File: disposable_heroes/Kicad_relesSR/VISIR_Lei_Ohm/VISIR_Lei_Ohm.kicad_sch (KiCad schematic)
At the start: 4 parts, among them K1 3572-1220-053

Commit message: update kicad
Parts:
- removed K1: 3572-1220-053, RELAY8_3572-1220-053_COM, symbol rele_DPST_Tese:3572-1220-053
- added J1: Raspberry_Pi_2_3, symbol Connector:Raspberry_Pi_2_3
- added K1: 3572-1220-123, RELAY8_3572-1220-053_COM, symbol 3572-1220-123:3572-1220-123
- added U1: 4N35, Package_DIP:DIP-6_W7.62mm, symbol Isolator:4N35
- added U2: ULN2003, symbol Transistor_Array:ULN2003
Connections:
- net at R2.1, R3.1: now also K1.8; no longer R1.1
- new net: K1.14, R1.1
- new net: K1.1, R1.2
- new net: K1.6, U2.16 (O1)
- new net: K1.7, R2.2
- new net +12V: K1.2, U2.9 (COM)
- new net GND: U2.8 (GND)
- now unconnected: R3.2
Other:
- moved on the sheet: R1, R2, R3

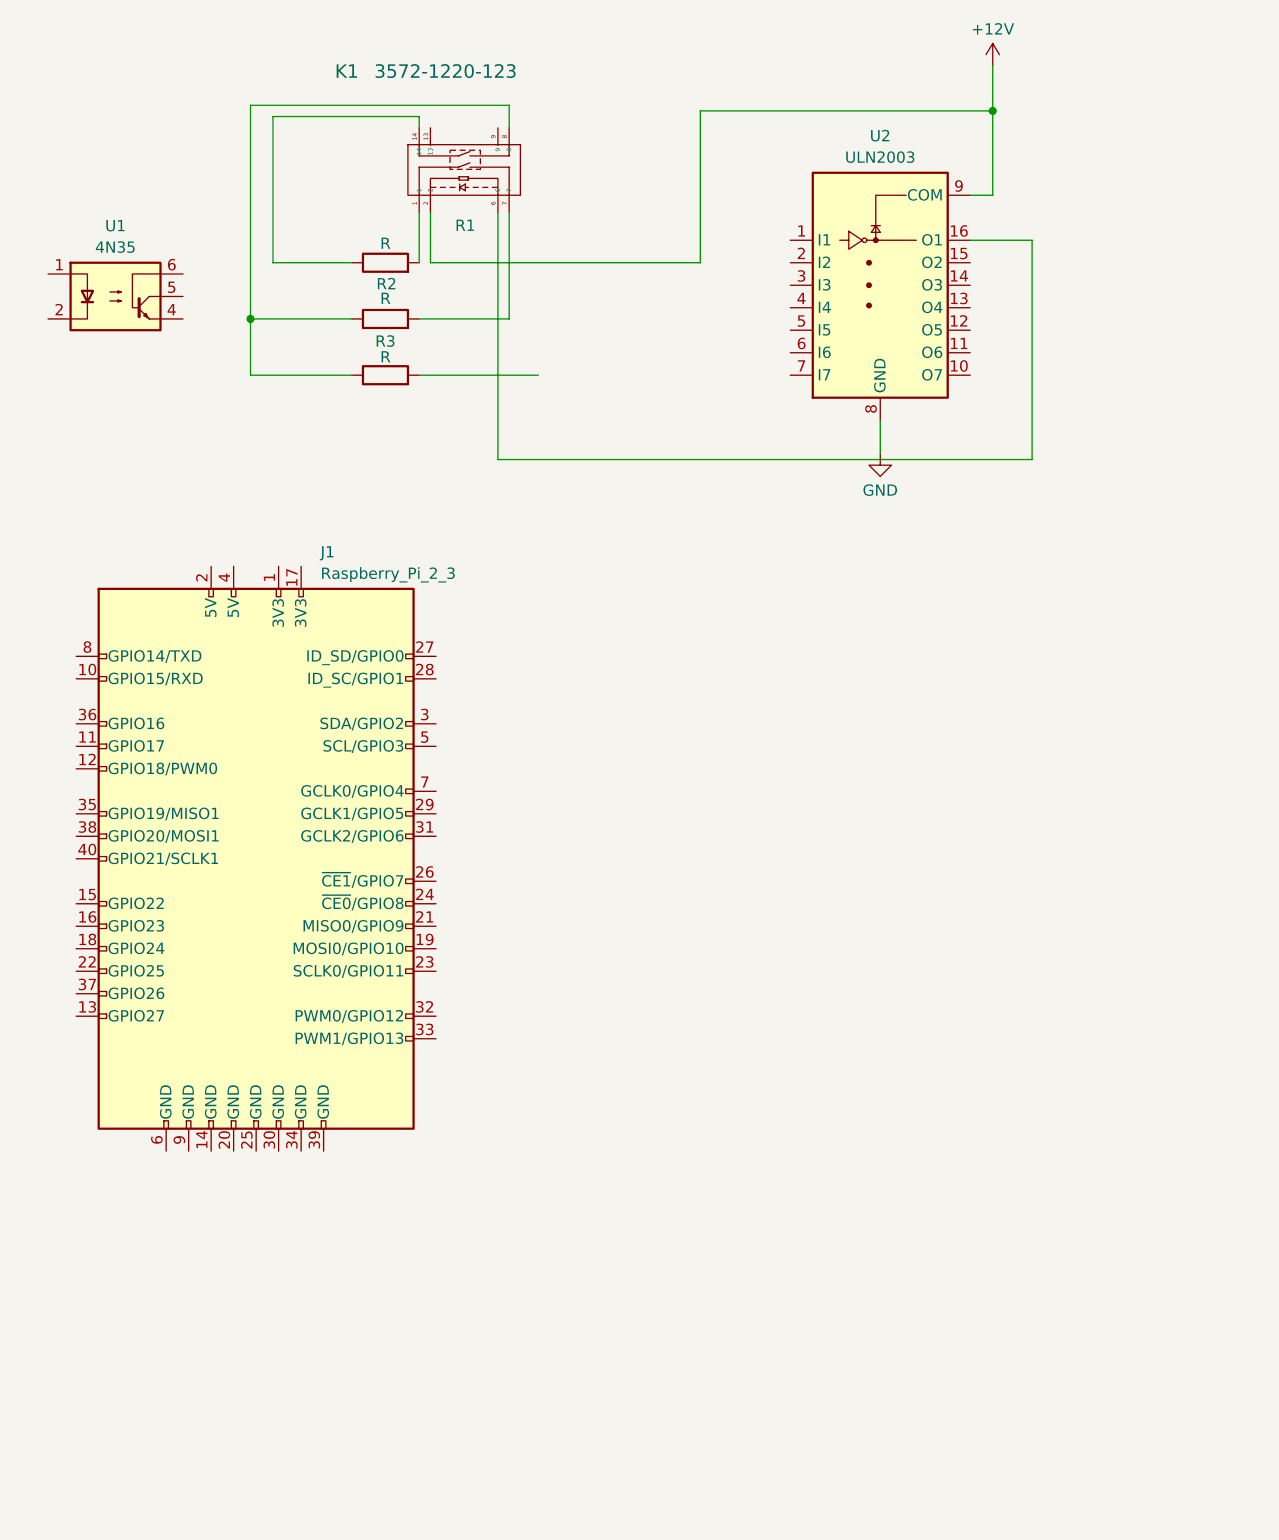
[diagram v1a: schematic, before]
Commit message: Kicad_Lei de Ohm
Parte do esquema de comando da Lei de Ohm
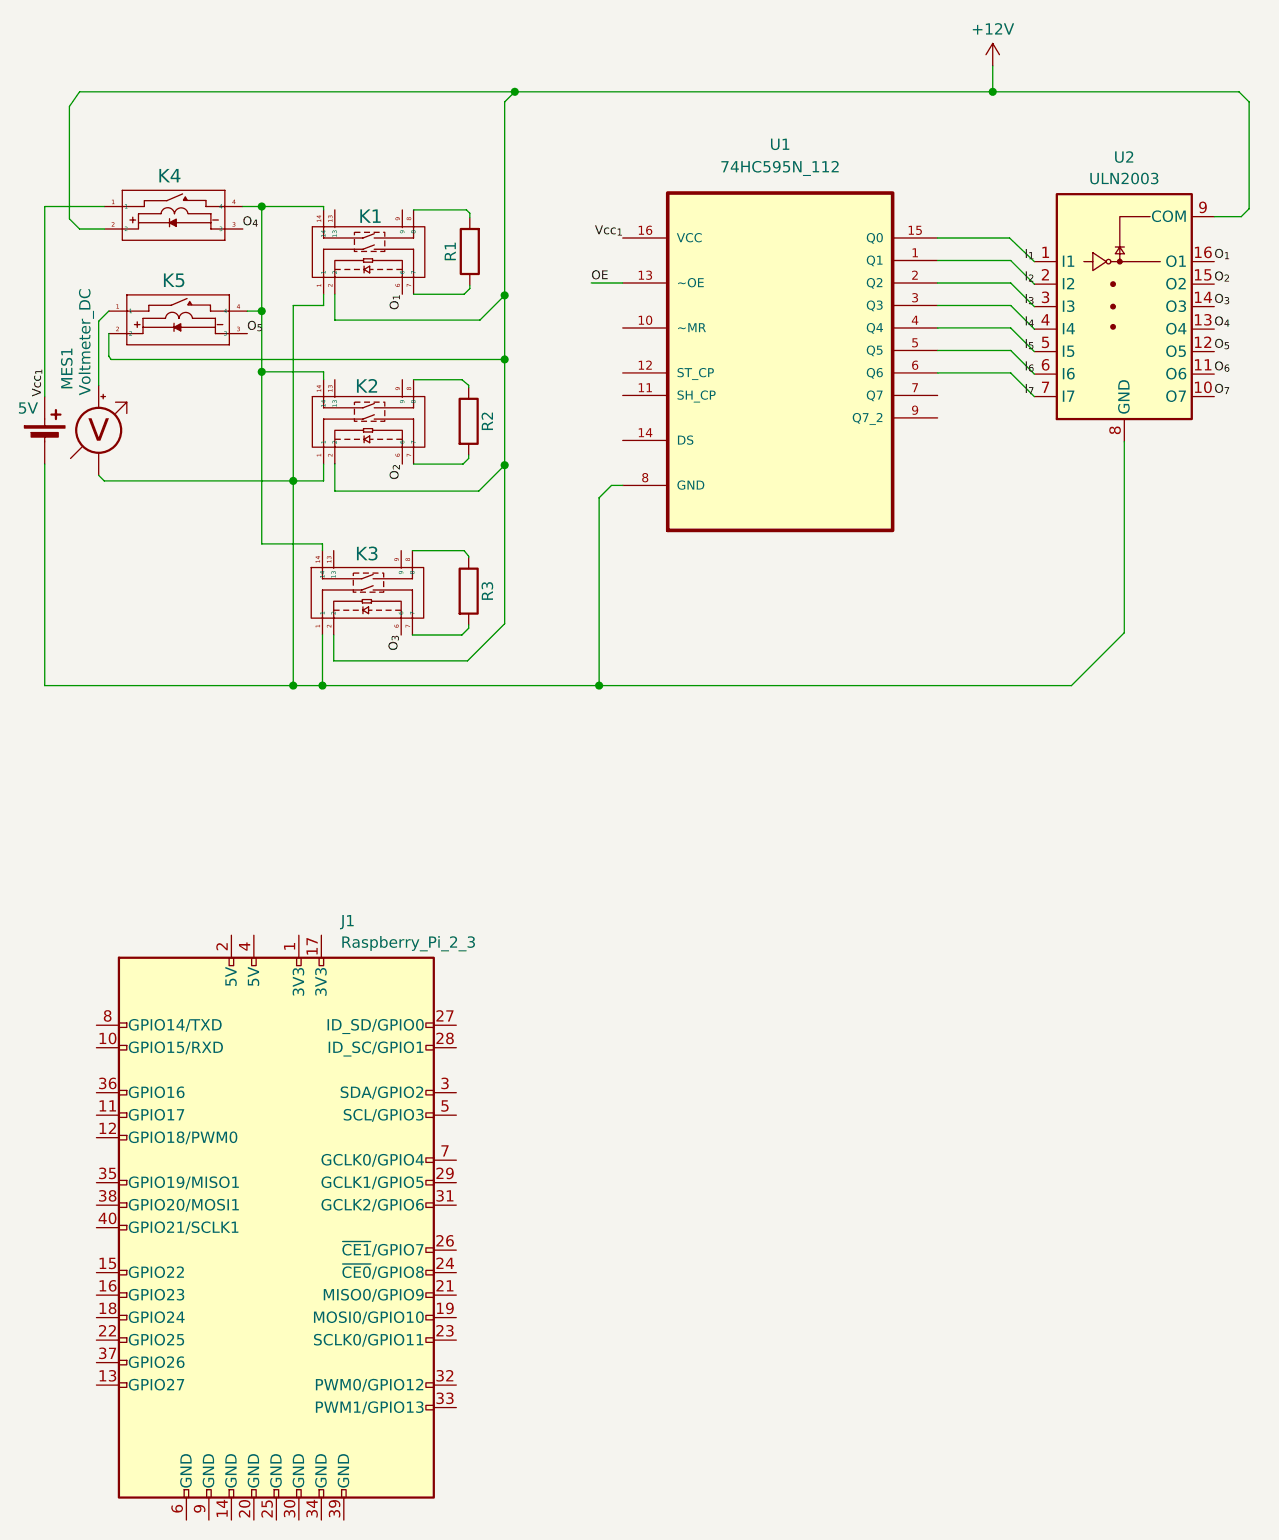
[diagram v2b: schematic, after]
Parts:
- removed U1: 4N35, Package_DIP:DIP-6_W7.62mm, symbol Isolator:4N35
- added K2, K3: 3572-1220-123, rele_DPST_tese:RELAY8_3572-1220-053_COM, symbol 3572-1220-123:3572-1220-123
- added K4, K5: 3570-1331-123, rele_SPST_tese:SIP_3570-1331_COM, symbol 3570-1331-123:3570-1331-123
- added MES1: Voltmeter_DC, Connector_PinHeader_2.54mm:PinHeader_1x02_P2.54mm_Vertical, symbol Device:Voltmeter_DC
- added U1: 74HC595N_112, Package_DIP:DIP-16_W10.16mm, symbol 74HC595N:74HC595N_112
- added Vcc1: 5V, Connector_PinHeader_2.54mm:PinHeader_1x02_P2.54mm_Vertical, symbol Device:Battery_Cell
- J1: footprint (none) -> Connector_PinHeader_2.54mm:PinHeader_2x39_P2.54mm_Vertical
- K1: footprint RELAY8_3572-1220-053_COM -> rele_DPST_tese:RELAY8_3572-1220-053_COM
- R1: value R -> R1; footprint (none) -> Resistor_THT:R_Axial_DIN0207_L6.3mm_D2.5mm_P15.24mm_Horizontal
- R2: value R -> R2; footprint (none) -> Resistor_THT:R_Axial_DIN0207_L6.3mm_D2.5mm_P15.24mm_Horizontal
- R3: value R -> R3; footprint (none) -> Resistor_THT:R_Axial_DIN0207_L6.3mm_D2.5mm_P15.24mm_Horizontal
- U2: footprint (none) -> Package_DIP:DIP-16_W10.16mm
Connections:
- net +12V: now also K2.2, K3.2, K4.2, K5.2
- net at R1.1: now also K1.7; no longer K1.14
- net at R1.2: now also K1.8; no longer K1.1
- net I_{1}: now reaches U2.1 (I1)
- net I_{1}: now also U1.15 (Q0)
- net O_{7}: now reaches U2.10 (O7)
- net O_{6}: now reaches U2.11 (O6)
- net O_{5}: now reaches U2.12 (O5)
- net O_{4}: now reaches U2.13 (O4)
- net O_{3}: now reaches U2.14 (O3)
- net O_{3}: now also K3.6
- net O_{2}: now reaches U2.15 (O2)
- net O_{2}: now also K2.6
- net O_{1}: now reaches K1.6, U2.16 (O1)
- net I_{2}: now reaches U2.2 (I2)
- net I_{2}: now also U1.1 (Q1)
- net I_{3}: now reaches U2.3 (I3)
- net I_{3}: now also U1.2 (Q2)
- net I_{4}: now reaches U2.4 (I4)
- net I_{4}: now also U1.3 (Q3)
- net I_{5}: now reaches U2.5 (I5)
- net I_{5}: now also U1.4 (Q4)
- net I_{6}: now reaches U2.6 (I6)
- net I_{6}: now also U1.5 (Q5)
- net I_{7}: now reaches U2.7 (I7)
- net I_{7}: now also U1.6 (Q6)
- net at R2.2: now also K2.7; no longer K1.7
- net at R3.2: now also K3.7
- net GND: no longer names the net of U2.8 (GND)
- net GND: now also K1.1, K2.1, K3.1, MES1.1 (-), U1.8 (GND), Vcc1.2 (-)
- new net: K5.1, MES1.2 (+)
- new net: K1.14, K2.14, K3.14, K4.4, K5.4
- new net: K3.8, R3.1
- new net: K2.8, R2.1
- new net OE: U1.13 (~OE)
- new net Vcc_{1}: K4.1, U1.16 (VCC), Vcc1.1 (+)
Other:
- moved on the sheet: J1, K1, U2

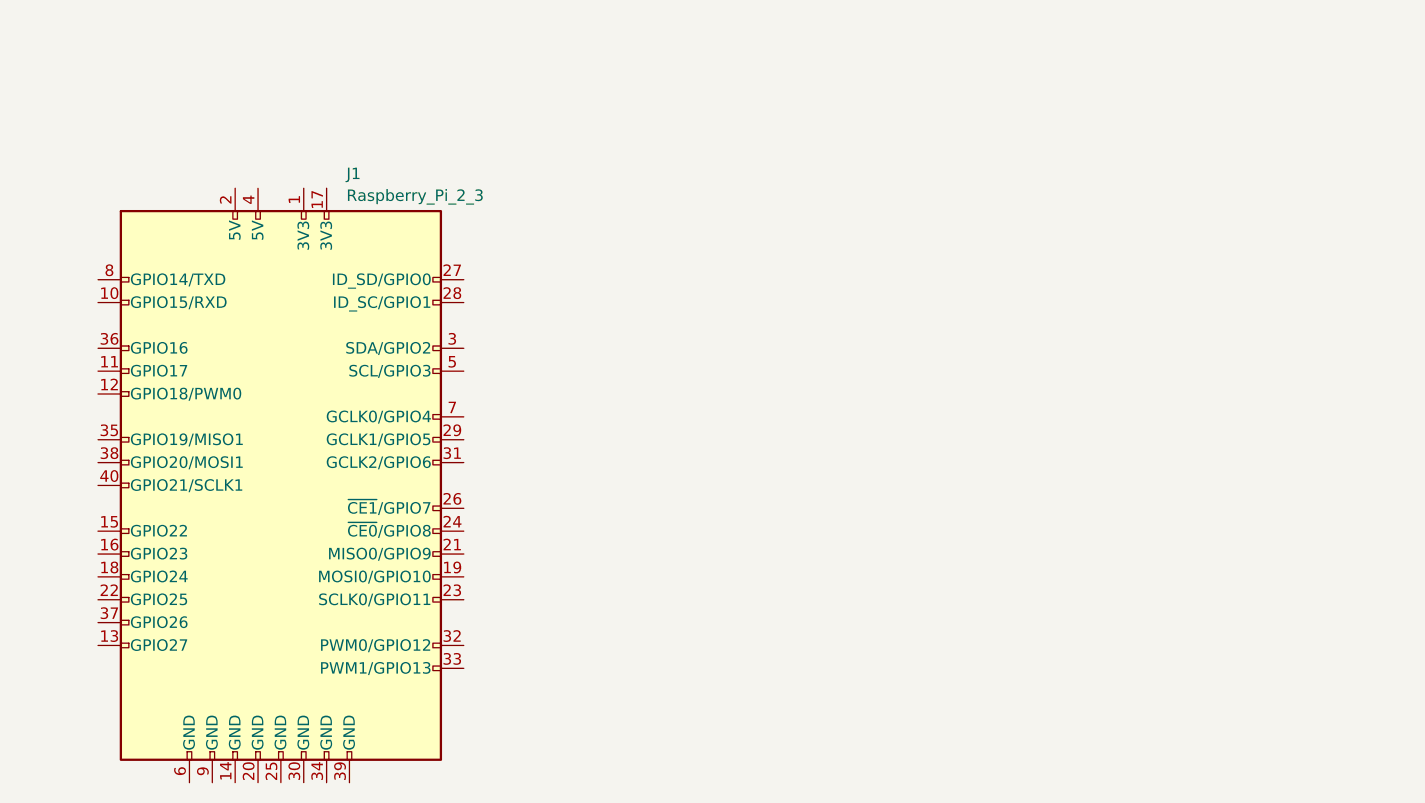
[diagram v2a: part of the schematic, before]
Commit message: kicad pi5 symbol
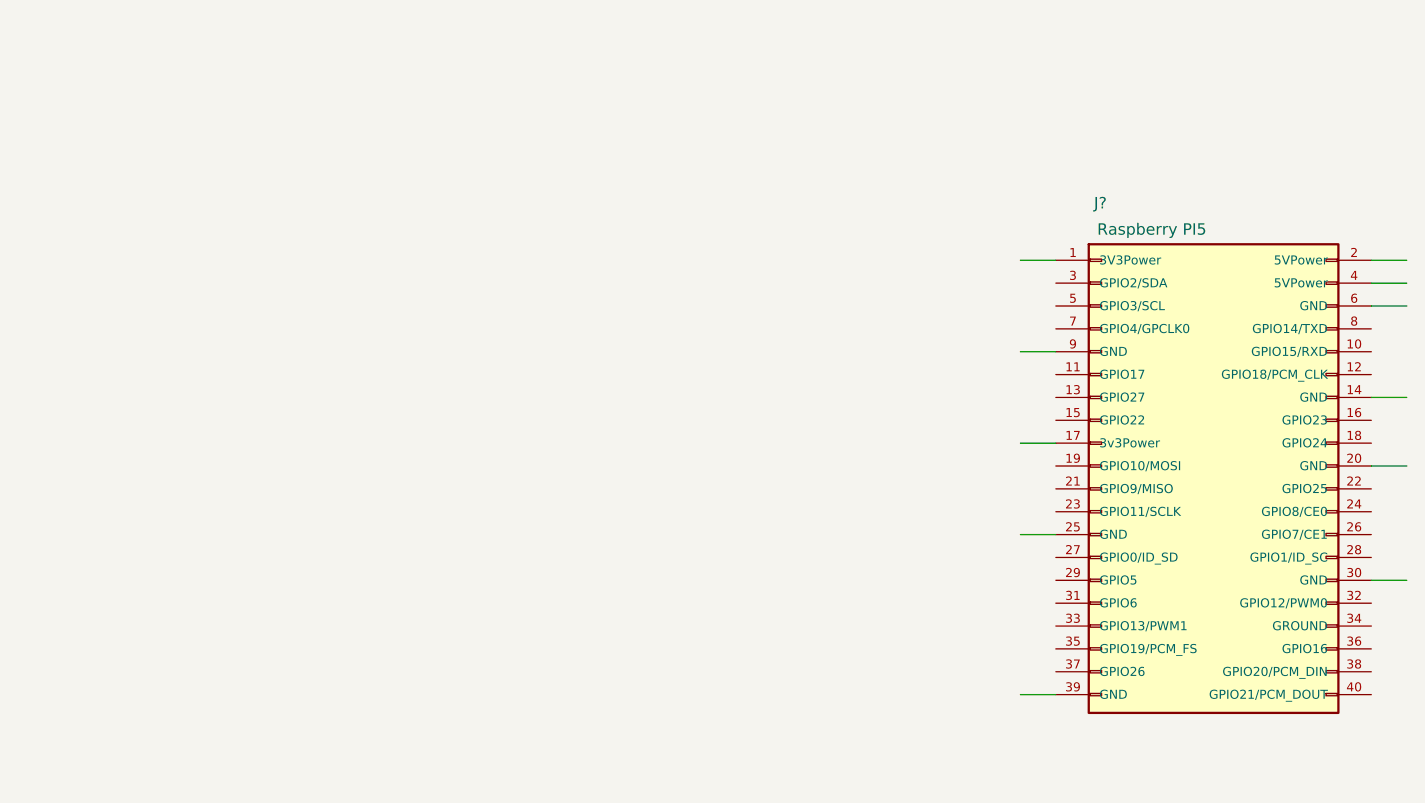
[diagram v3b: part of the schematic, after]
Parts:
- removed J1: Raspberry_Pi_2_3, Connector_PinHeader_2.54mm:PinHeader_2x39_P2.54mm_Vertical, symbol Connector:Raspberry_Pi_2_3
- added J?: Raspberry PI5, symbol PI5:Raspberry_PI5

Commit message: update kicad VISIR_Lei_Ohm
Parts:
- removed Vcc1: 5V, Connector_PinHeader_2.54mm:PinHeader_1x02_P2.54mm_Vertical, symbol Device:Battery_Cell
- added K6, K7, K8: 3570-1331-123, SIP_3570-1331_COM, symbol 3570-1331-123:3570-1331-123
- added MES2: Ammeter_DC, symbol Device:Ammeter_DC
- K5: footprint rele_SPST_tese:SIP_3570-1331_COM -> SIP_3570-1331_COM
- gave numbers to parts that had none: 1
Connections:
- net +12V: now also K7.2, K8.2
- net O_{4}: now also K4.3
- net O_{5}: now also K5.3
- net A: now reaches K5.1, MES1.2 (+)
- net A: now also K1.14, K2.14, K3.14, K4.4
- net GND: now reaches K3.1, MES1.1 (-), U1.8 (GND), U2.8 (GND)
- net GND: now also K7.4, K8.4; no longer K1.1, K2.1
- net ~{MR}: now reaches U1.10 (~MR)
- net SH_CP: now reaches U1.11 (SH_CP)
- net ST_CP: now reaches U1.12 (ST_CP)
- net DS: now reaches U1.14 (DS)
- net OE renamed ~{OE}
- net Vcc_{1} renamed +5V
- new net: K6.1, K6.2, MES2.2 (+)
- new net: K7.1, MES2.1 (-)
- new net B: K1.1, K2.1, K5.4, K6.4, K8.1
- new net O6: K6.3
- new net O7: K7.3
- new net O8: K8.3
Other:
- moved on the sheet: K5, MES1, U2
